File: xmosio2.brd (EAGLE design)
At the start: 116.8 x 55.2 mm, 103 parts, among them IC1 IDTQS3245QSOP20, IC2 IDTQS3245QSOP20, IC3 IDTQS3245QSOP20, IC4 IDTQS3245QSOP20, IC5 IDTQS3245QSOP20, U1 24 MHz Osc. (F535L-24), U2 USD-SOCKETNEW, X1 0446200002, X2 MINI-USB-UX60-MB-5S8

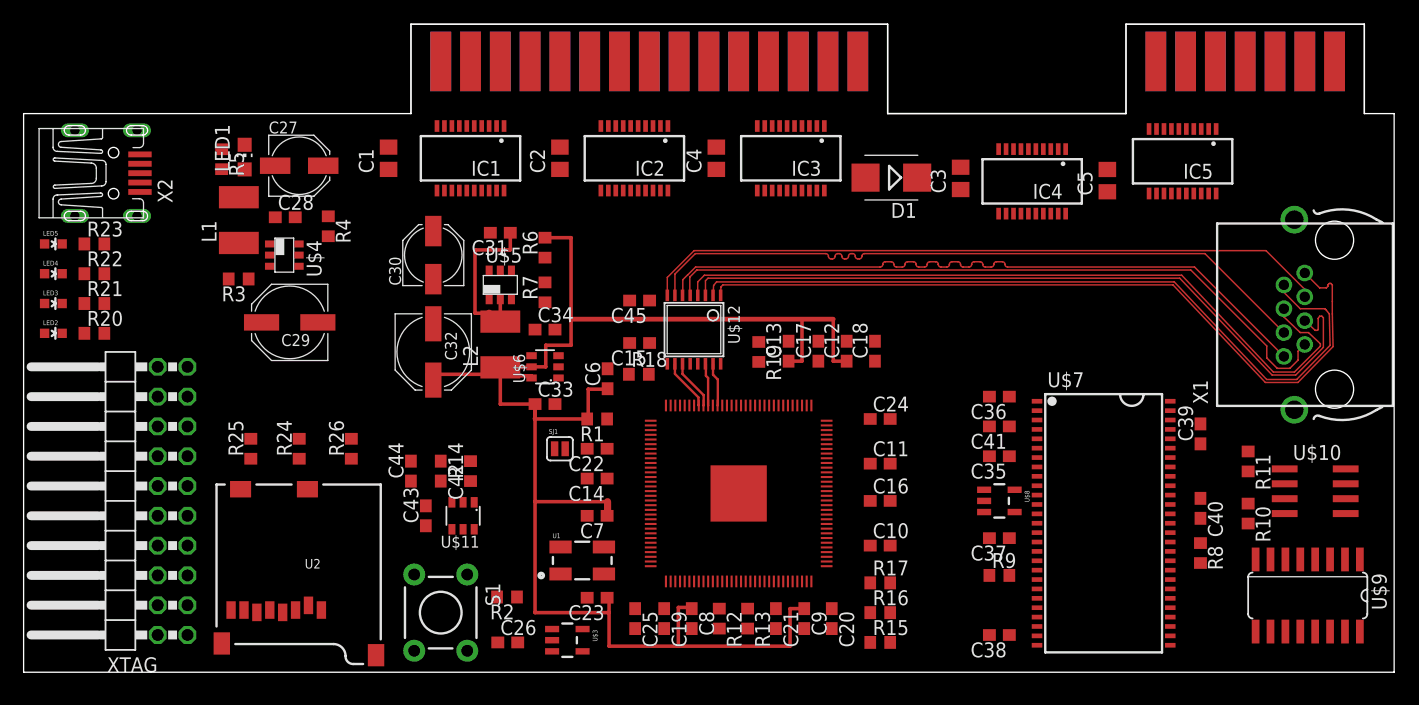
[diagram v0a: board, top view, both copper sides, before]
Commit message: Latest revision. Fixes:  - Rename the power line from 4.1 to 4.3v  - Make +5v be the only one with a specified width to aid in routing. The PCB traces are sufficiently wide, given they’re in air, and there are multiple supplies to the main chip  - Added the required vias on the ground pad of the XMOS chip  - Make LEDs be 0805 rather than 0603  - Fixes identified by Xcore.com user eez-open  - Fix connection of 1v converter EN to +5V  - Route JTAG lines and make Link lines pass DRC  - Add an SD card  - Add LEDs for debugging later  - Add a switch so that firmware can be booted from a golden master, rather than the latest on-board
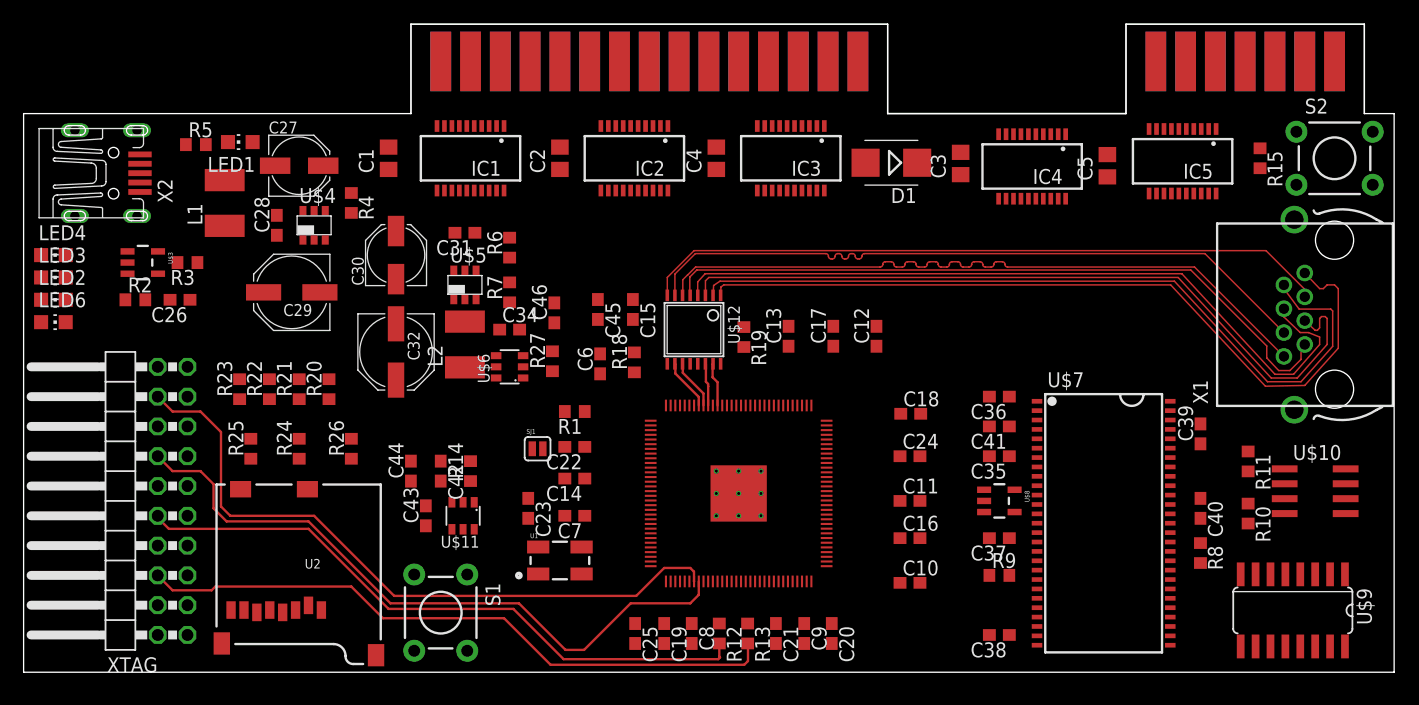
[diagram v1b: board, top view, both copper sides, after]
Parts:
- removed C33: 100nF, rcl:C0603
- removed LED5: (no value), SparkFun-LED:LED-0603
- removed R16, R17: 10K, rcl:R0603
- added C46: 100nF, rcl:C0603
- added LED6: ok33, led:CHIP-LED0805
- added R27: 47K, rcl:R0603
- added S2: FLASH_MODE, SparkFun:TACTILE-PTH
- LED2, LED3, LED4: value (none) -> ok33; device SparkFun-LED:LED-0603 -> led:CHIP-LED0805
- moved R15 52.5 mm to (105.4, 43.8), turned to 270 degrees
- moved U$3 48.4 mm to (10.2, 34.9)
- moved R2 40.6 mm to (9.53, 31.8), turned to 0 degrees
- moved C26 40.4 mm to (13.3, 31.8), turned to 180 degrees
- moved R20 20.6 mm to (26.0, 24.1), turned to 90 degrees
- moved R21 18.9 mm to (23.5, 24.1), turned to 90 degrees
- moved R22 17.9 mm to (21.0, 24.1), turned to 90 degrees
- moved R23 17.5 mm to (18.4, 24.1), turned to 90 degrees
- moved C23 9.62 mm to (43.0, 14.0), turned to 270 degrees
- moved C18 6.14 mm to (75.6, 22.0), turned to 0 degrees
- moved R3 4.58 mm to (14.0, 34.9)
- moved C11 4.07 mm to (75.6, 14.6)
- moved C16 4.07 mm to (75.6, 11.4)
- moved C24 4.07 mm to (75.6, 18.4)
- moved C10 4.07 mm to (75.6, 7.62)
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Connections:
- net +4.1V renamed +4.3V
- new net EN_1V0: R27.1, U$5.5, U$6.1
- net +5V: no longer U$5.5, U$6.1
- net GND: now also C46.2, S2.3, S2.4; no longer C33.2, R15.2, R16.2, R17.2
- net LED0: now also LED6.A; no longer LED2.A
- net LED1: now also LED2.A; no longer LED3.A
- net LED2: now also LED3.A; no longer LED4.A
- net LED3: now also LED4.A; no longer LED5.A
- net N$10: now also LED1.C; no longer LED1.A
- net N$24: now also LED4.C; no longer LED5.C
- net N$25: now also LED3.C; no longer LED4.C
- net N$26: now also LED2.C; no longer LED3.C
- net N$27: now also LED6.C; no longer LED2.C
- net N$33: now also R15.1, S2.1, S2.2
- net SD_ADQ2/QS_D0: no longer R15.1
- net SD_ADQ3/QS_D1: no longer R16.1
- net SD_ADQ4/QS_D2: no longer R17.1
- net VCCINT: no longer C33.1, U$6.6
- net VCCIO: now also C46.1, LED1.A, R15.2, R27.2, U$6.6; no longer LED1.C
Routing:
- net VCCINT: track 138.2 -> 0.00 mm
- net JTAG_DN1: track 0.00 -> 58.4 mm
- net JTAG_DN0: track 0.00 -> 57.3 mm
- net JTAG_UP1: track 0.00 -> 55.4 mm
- net JTAG_UP0: track 0.00 -> 54.4 mm
- net N$11: track 14.6 -> 0.00 mm
- net RIN1_N: track 66.3 -> 67.3 mm
- net RIN1_P: track 66.3 -> 67.3 mm
- net RIN2_P: track 64.1 -> 64.9 mm
- net RIN2_N: track 63.9 -> 64.4 mm

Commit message: Tidy up the board labelling
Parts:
- removed S1: MANUAL_RESET, SparkFun:TACTILE-PTH
- removed S2: FLASH_MODE, SparkFun:TACTILE-PTH
- added BOOT_SW: FLASH_MODE, SparkFun:TACTILE-PTH
- added RESET_SW: MANUAL_RESET, SparkFun:TACTILE-PTH
- moved R6 0.95 mm to (41.4, 37.1)
- moved R15 0.90 mm to (104.8, 43.2)
- moved R27 0.79 mm to (45.1, 25.7)
- moved R18 0.70 mm to (52.1, 25.7)
- moved U$6 0.64 mm to (41.4, 25.4)
- moved C23 0.63 mm to (43.0, 14.6)
- moved C28 0.63 mm to (21.6, 38.7)
- moved C6 0.63 mm to (48.9, 25.7)
- moved C18 0.51 mm to (75.6, 22.5)
- moved R19 0.37 mm to (61.6, 28.9)
- moved C24 0.32 mm to (75.6, 18.7)
- moved C44 0.32 mm to (32.7, 17.1)
- moved C11 0.32 mm to (75.6, 14.9)
- moved C46 0.32 mm to (45.2, 31.0)
- moved C13 0.32 mm to (65.4, 28.9)
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- renumbered LED2 to DBG1, LED3 to DBG2, LED4 to DBG3, LED6 to DBG0, X2 to USBPOWER
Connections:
- net GND: now also BOOT_SW.3, BOOT_SW.4, RESET_SW.3, RESET_SW.4; no longer S1.3, S1.4, S2.3, S2.4
- net N$21: now also RESET_SW.1, RESET_SW.2; no longer S1.1, S1.2
- net N$33: now also BOOT_SW.1, BOOT_SW.2; no longer S2.1, S2.2
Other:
- board text added: "SD_CARD"
